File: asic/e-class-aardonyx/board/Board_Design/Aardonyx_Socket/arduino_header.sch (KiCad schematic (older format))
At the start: 35 parts, among them J10 Conn_1x6, J11 Conn_1x6, J12 Conn_1x3_M, J13 Conn_1x8_F, J14 Conn_1x6_F, J15 Conn_1x10_F, J16 Conn_1x8_F, J19 Conn_1x3_M, J7 Conn_1x4, J8 Conn_1x3_M, J9 Conn_1x8, U5 CAT24M01WI-GT3, U6 IS25LP256x-xM, U7 ADC128S102CIMTX/NOPB, U8 LSF0108PWR, U9 LSF0108PWR

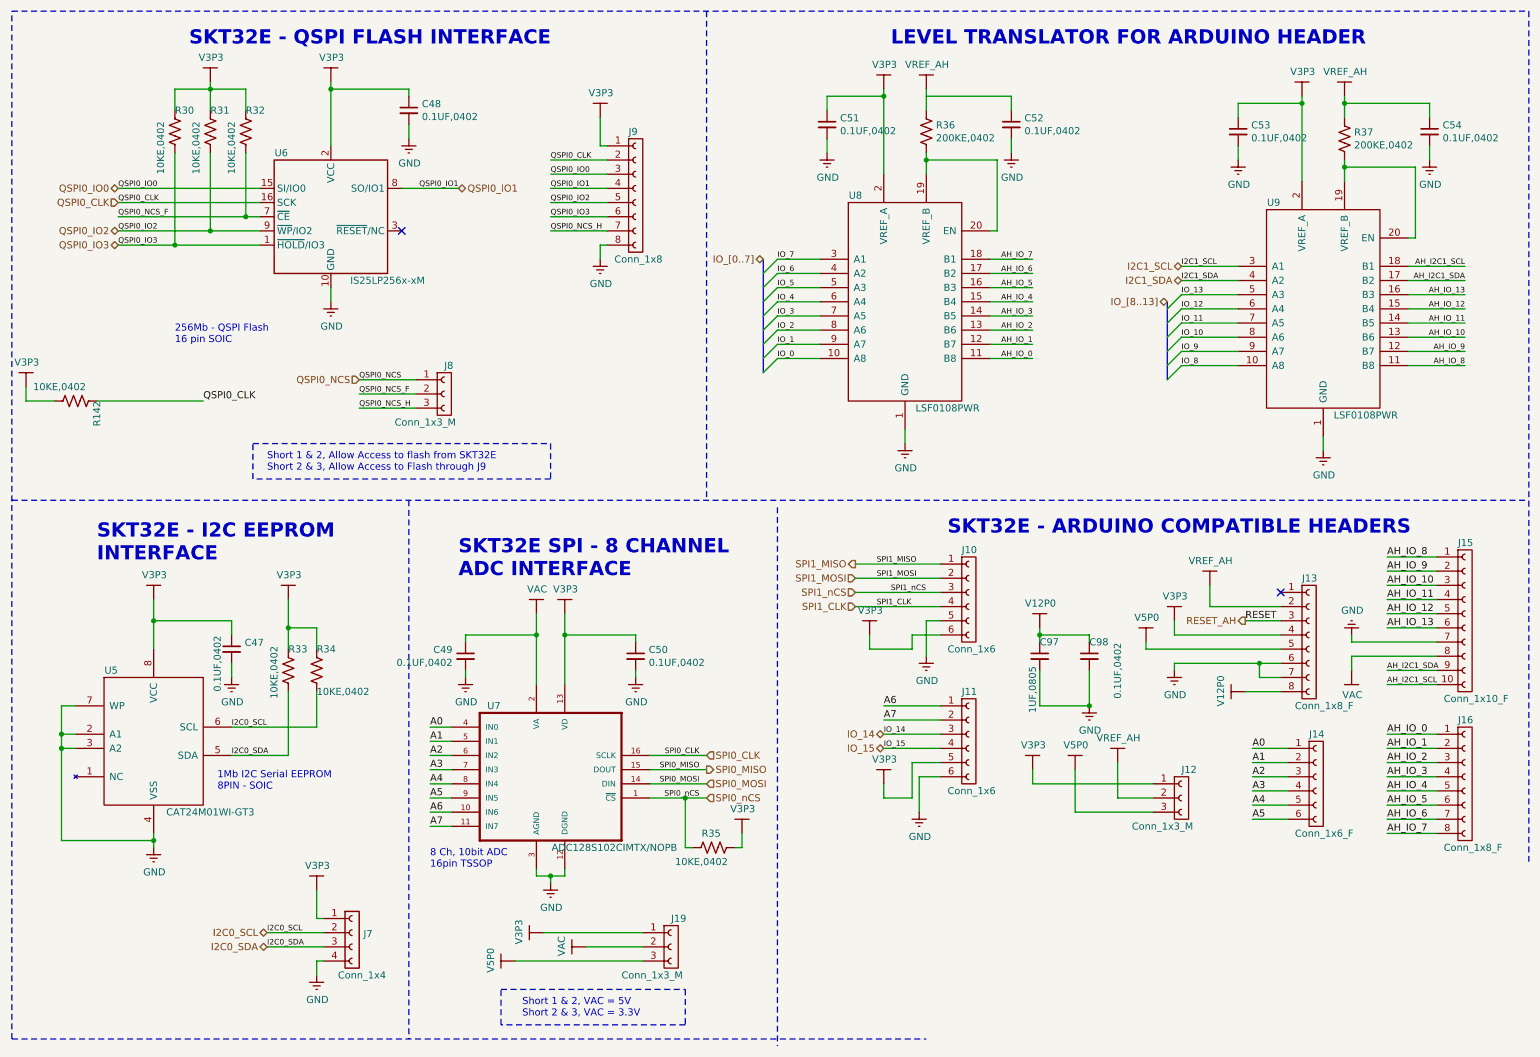
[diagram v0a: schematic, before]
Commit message: update socket compo placement
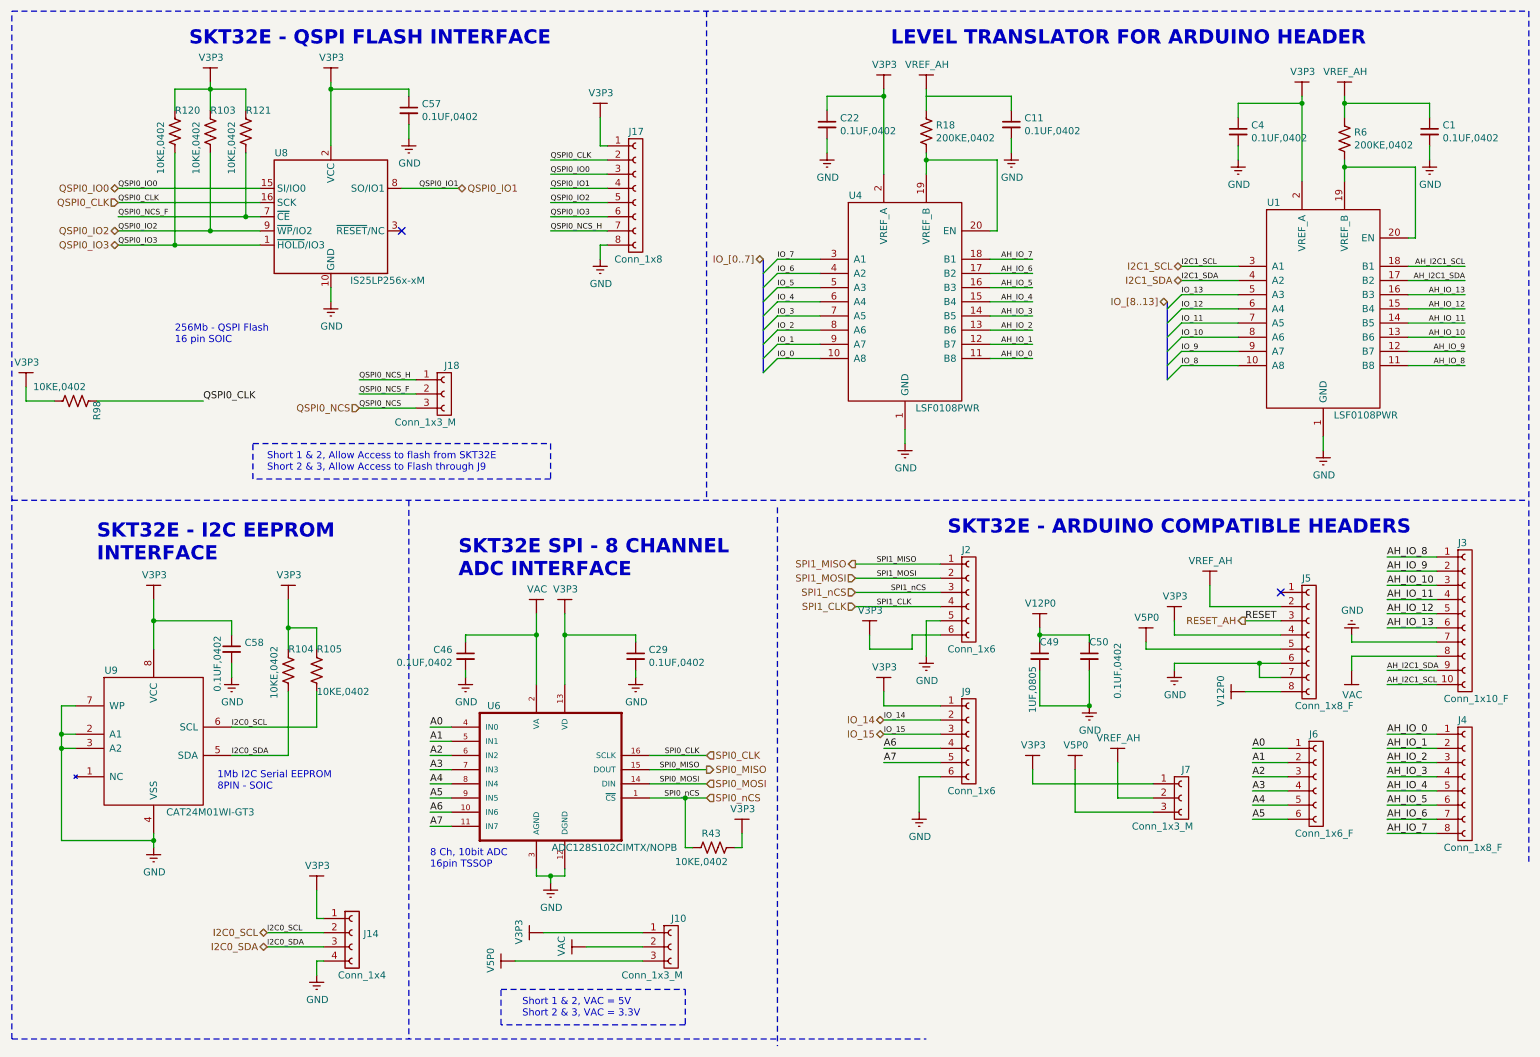
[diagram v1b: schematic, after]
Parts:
- renumbered C54 to C1, C52 to C11, C51 to C22, C50 to C29, C53 to C4, C49 to C46, C97 to C49, C98 to C50, C48 to C57, C47 to C58, J19 to J10, J7 to J14, J9 to J17, J8 to J18, J10 to J2, J15 to J3, J16 to J4, J13 to J5, J14 to J6, J12 to J7, J11 to J9, R31 to R103, R33 to R104, R34 to R105, R30 to R120, R32 to R121, R36 to R18, R35 to R43, R37 to R6, R142 to R98, U9 to U1, U8 to U4, U7 to U6, U6 to U8, U5 to U9
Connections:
- net A6: now also J9.4 (Pin_4); no longer J9.1 (Pin_1)
- net A7: now also J9.5 (Pin_5); no longer J9.2 (Pin_2)
- net IO_14: now also J9.2 (Pin_2); no longer J9.3 (Pin_3)
- net IO_15: now also J9.3 (Pin_3); no longer J9.4 (Pin_4)
- net QSPI0_NCS: now also J18.3 (Pin_3); no longer J18.1 (Pin_1)
- net QSPI0_NCS_H: now also J18.1 (Pin_1); no longer J18.3 (Pin_3)
- net V3P3: now also J9.1 (Pin_1); no longer J9.5 (Pin_5)

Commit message: updated soc back annotation
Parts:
- U9: footprint Package_SO:SOIC-8_3.9x4.9mm_P1.27mm -> Package_SO:SOIC-8_5.23x5.23mm_P1.27mm
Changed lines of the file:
@@
 F 0 "U9" H 1200 6150 50  0000 C CNN
 F 1 "CAT24M01WI-GT3" H 1900 5150 50  0000 C CNN
-F 2 "Package_SO:SOIC-8_3.9x4.9mm_P1.27mm" H 1500 5650 50  0001 C CNN
+F 2 "Package_SO:SOIC-8_5.23x5.23mm_P1.27mm" H 1500 5650 50  0001 C CNN
 F 3 "https://www.digikey.in/product-detail/en/on-semiconductor/CAT24M01WI-GT3/CAT24M01WI-GT3OSCT-ND/2698362" H 1500 5650 50  0001 C CNN
 F 4 "IC EEPROM 1M I2C 1MHZ 8SOIC" H 1500 5650 50  0001 C CNN "Description"

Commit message: Back annotation
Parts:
- renumbered C29 to C11, C46 to C23, C1 to C3, C49 to C32, C50 to C36, C4 to C5, C11 to C7, C58 to C75, C57 to C76, C22 to C8, J2 to J1, J14 to J16, J3 to J2, J4 to J3, J5 to J4, J6 to J5, J9 to J8, J10 to J9, R104 to R128, R105 to R129, R98 to R130, R103 to R131, R120 to R132, R121 to R133, R18 to R25, R43 to R39, R6 to R9, U9 to U11, U8 to U12, U1 to U2, U6 to U5
